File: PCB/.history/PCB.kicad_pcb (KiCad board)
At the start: 2 copper layers, 139 x 123.8 mm, 87 parts, among them J1 USB_C_Receptacle_USB2.0_14P, J2 OLED_128x64, SW1 SW_Push, SW2 RotaryEncoder, SW3 RotaryEncoder, U1 STM32F072CBTx, U2 USBLC6-2SC6, U3 XC6206, U5 TRRS

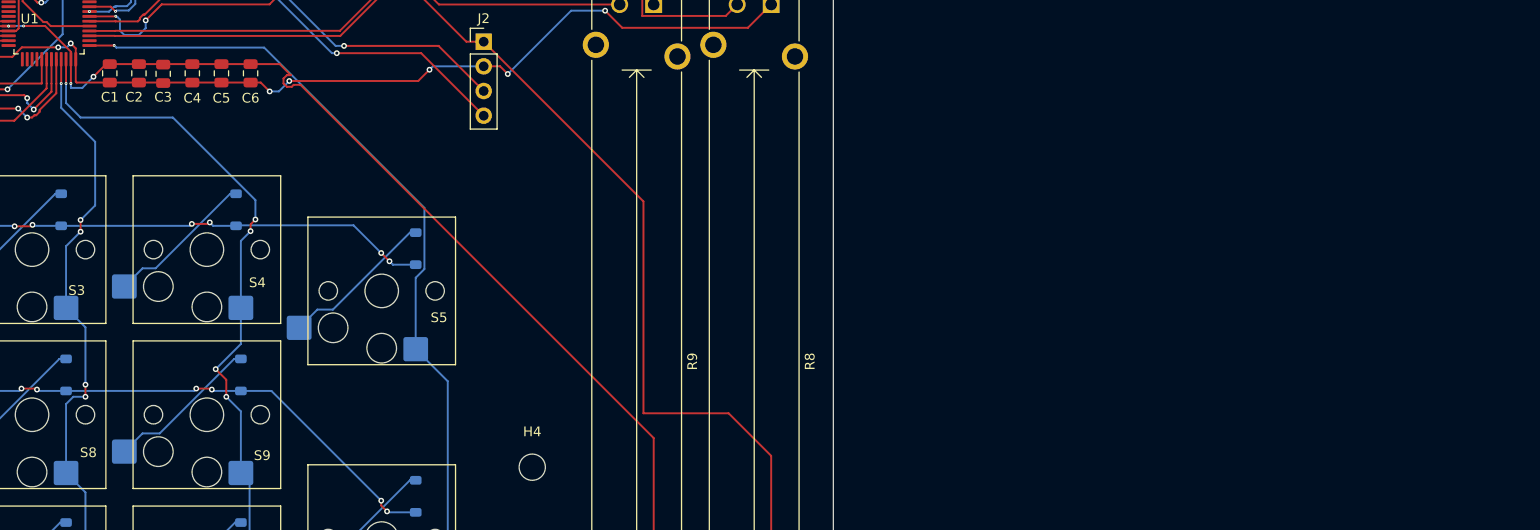
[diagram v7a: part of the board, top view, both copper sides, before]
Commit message: Added sd card and fixed some wirings
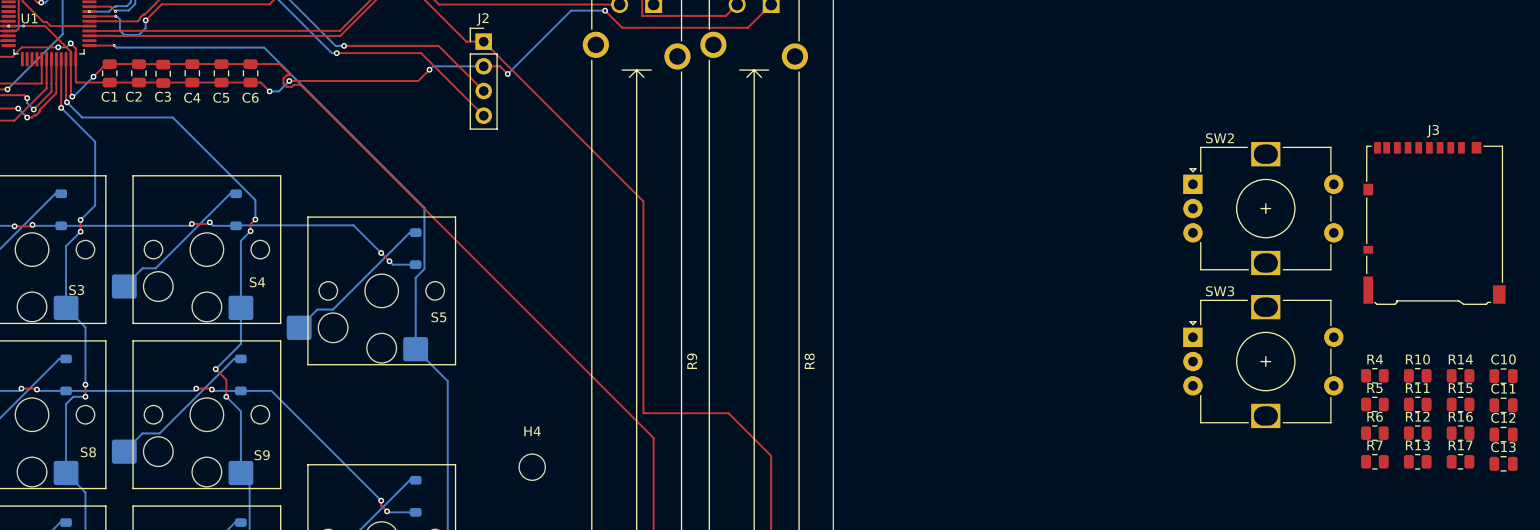
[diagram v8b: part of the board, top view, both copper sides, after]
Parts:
- added C10: 10nF, Capacitor_SMD:C_0805_2012Metric, F.Cu at (235.5, 87.1)
- added C11: 10nF, Capacitor_SMD:C_0805_2012Metric, F.Cu at (235.5, 90.1)
- added C12: 10nF, Capacitor_SMD:C_0805_2012Metric, F.Cu at (235.5, 93.1)
- added C13: 10nF, Capacitor_SMD:C_0805_2012Metric, F.Cu at (235.5, 96.2)
- added J3: Micro_SD_Card_Det1, Connector_Card:microSD_HC_Hirose_DM3AT-SF-PEJM5, F.Cu at (228.4, 71.3)
- added R10: 10k, Resistor_SMD:R_0805_2012Metric, F.Cu at (226.7, 87.1)
- added R11: 10k, Resistor_SMD:R_0805_2012Metric, F.Cu at (226.7, 90.0)
- added R12: 10k, Resistor_SMD:R_0805_2012Metric, F.Cu at (226.7, 93.0)
- added R13: 10k, Resistor_SMD:R_0805_2012Metric, F.Cu at (226.7, 95.9)
- added R14: 10k, Resistor_SMD:R_0805_2012Metric, F.Cu at (231.1, 87.1)
- added R15: 10k, Resistor_SMD:R_0805_2012Metric, F.Cu at (231.1, 90.0)
- added R16: 10k, Resistor_SMD:R_0805_2012Metric, F.Cu at (231.1, 93.0)
- added R17: 10k, Resistor_SMD:R_0805_2012Metric, F.Cu at (231.1, 95.9)
- added R4: 10k, Resistor_SMD:R_0805_2012Metric, F.Cu at (222.3, 87.1)
- added R5: 10k, Resistor_SMD:R_0805_2012Metric, F.Cu at (222.3, 90.0)
- added R6: 10k, Resistor_SMD:R_0805_2012Metric, F.Cu at (222.3, 93.0)
- added R7: 10k, Resistor_SMD:R_0805_2012Metric, F.Cu at (222.3, 95.9)
- added SW2: RotaryEncoder, Rotary_Encoder:RotaryEncoder_Alps_EC12E-Switch_Vertical_H20mm, F.Cu at (203.5, 67.4)
- added SW3: RotaryEncoder, Rotary_Encoder:RotaryEncoder_Alps_EC12E-Switch_Vertical_H20mm, F.Cu at (203.5, 83.1)
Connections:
- U1 pad 12: unconnected-(U1-PA2-Pad12) -> SLIDER_2
- U1 pad 13: unconnected-(U1-PA3-Pad13) -> SLIDER_1
- U1 pad 14: unconnected-(U1-PA4-Pad14) -> CS
- U1 pad 15: unconnected-(U1-PA5-Pad15) -> IS_SD
- U1 pad 26: unconnected-(U1-PB13-Pad26) -> SCK
- U1 pad 27: SLIDER_1 -> MISO
- U1 pad 28: SLIDER_2 -> MOSI
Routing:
- net GND: track 508.6 -> 509.8 mm
